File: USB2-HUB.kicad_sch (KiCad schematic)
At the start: 31 parts, among them J1 USB_OTG, J2 690-008-221-904, U1 FSUSB42MUX, U2 USB2514B-I/M2, U3 TPD4EUSB30, U4 AP22653W6, Y1 24MHz

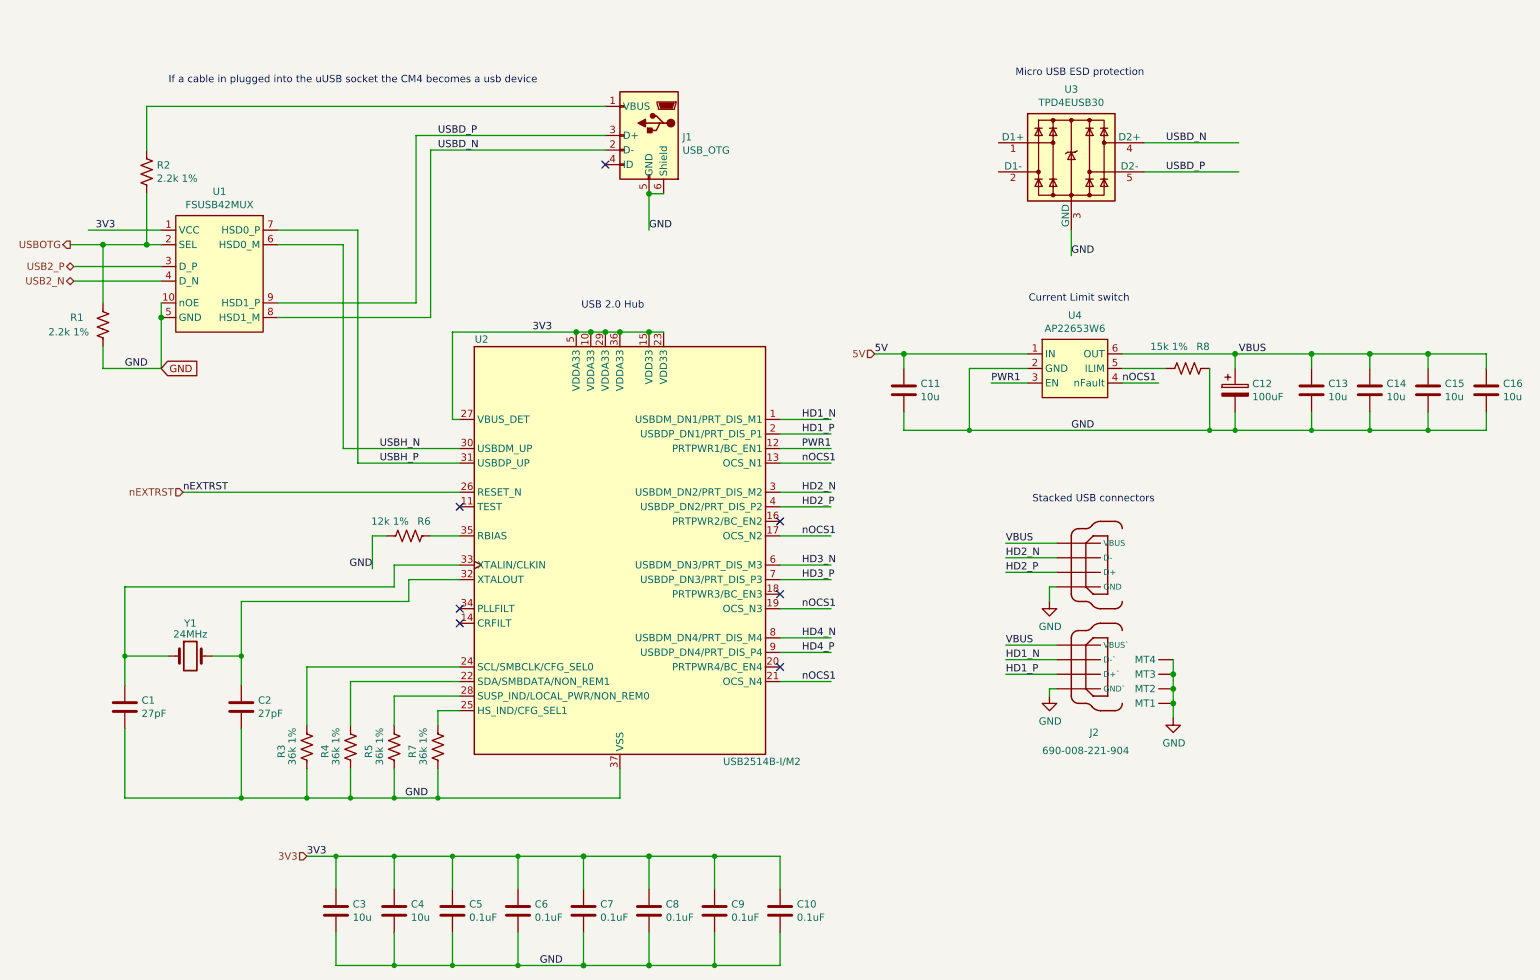
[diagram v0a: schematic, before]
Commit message: added more USB ports.. placing
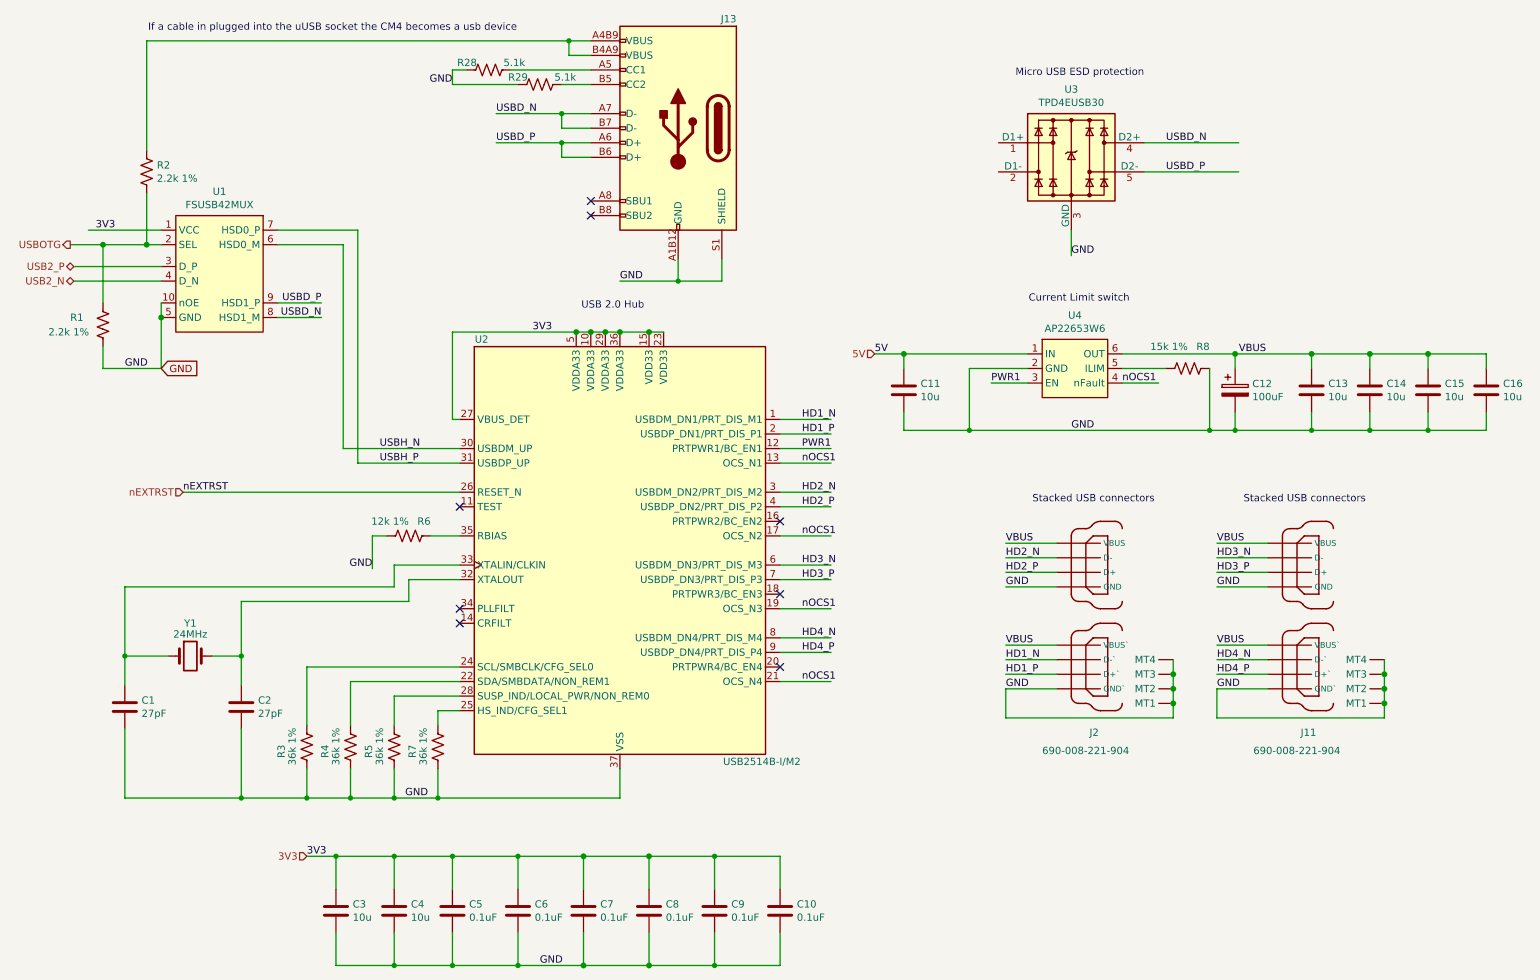
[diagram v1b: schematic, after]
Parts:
- removed J1: USB_OTG, CM4IO:USB_Micro-B_EDAC_UCON00686, symbol Connector:USB_OTG
- added J11: 690-008-221-904, CM4IO:MOLEX_USB_67298-4090, symbol CM4IO:USB_67298-4090
- added J13: USB_C_Receptacle_USB2.0, bitcart:USB_C_Receptacle_GCT_USB4105-xx-A_16P_TopMnt_Horizontal, symbol bitcart:USB_C_Receptacle_USB2.0
- added R28, R29: 5.1k, Resistor_SMD:R_0402_1005Metric, symbol Device:R_US
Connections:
- net GND: now also J11.4 (GND`), J11.8 (GND), J11.MT1, J11.MT2, J11.MT3, J11.MT4, J13.A1B12 (GND), J13.B1A12 (GND), J13.S1 (SHIELD), R28.1, R29.1
- net HD3_N: now also J11.6 (D-)
- net HD3_P: now also J11.7 (D+)
- net HD4_N: now also J11.2 (D-`)
- net HD4_P: now also J11.3 (D+`)
- net USBD_N: now also J13.A7 (D-), J13.B7 (D-)
- net USBD_P: now also J13.A6 (D+), J13.B6 (D+)
- net VBUS: now also J11.1 (VBUS`), J11.5 (VBUS)
- net at R2.1: now also J13.A4B9 (VBUS), J13.B4A9 (VBUS)
- new net: J13.A5 (CC1), R28.2
- new net: J13.B5 (CC2), R29.2
- no-connect marks 7 -> 8
